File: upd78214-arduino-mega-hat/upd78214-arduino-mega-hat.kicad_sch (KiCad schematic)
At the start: 11 parts, among them J1 Power, J2 PWM, J3 Analog, J4 PWM, J5 Analog, J6 Communication, J7 Digital, U1 upd78214-64p-qfp, Y1 4-12MHz

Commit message: Rambling
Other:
- note added: "PROM read mode needs +12.5V on NMI, ~{RESET} low, ~{CE} and ~{OE} low"
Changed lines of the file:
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@@
+		)
+	)
+	(text "PROM read mode needs +12.5V on NMI, ~{RESET} low, ~{CE} and ~{OE} low"
+		(exclude_from_sim no)
+		(at 226.06 60.96 0)
+		(effects
+			(font
+				(size 1.27 1.27)
+			)
 		)
 	)

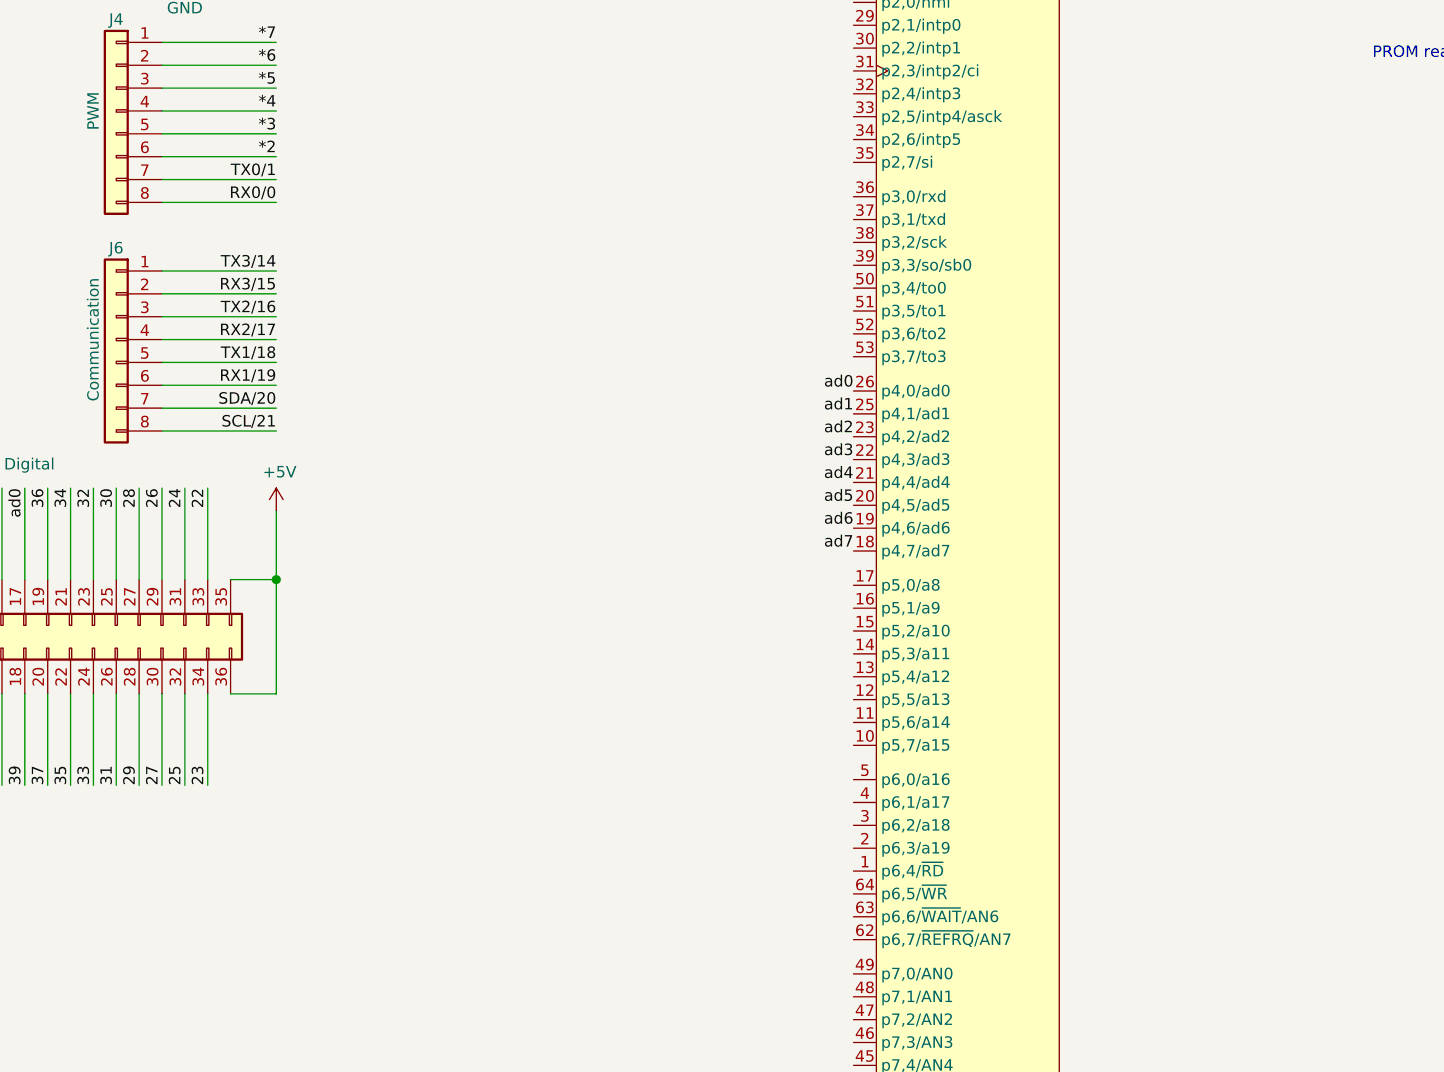
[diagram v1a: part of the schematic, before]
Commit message: TX/RX jumpers, enormous memory products data book
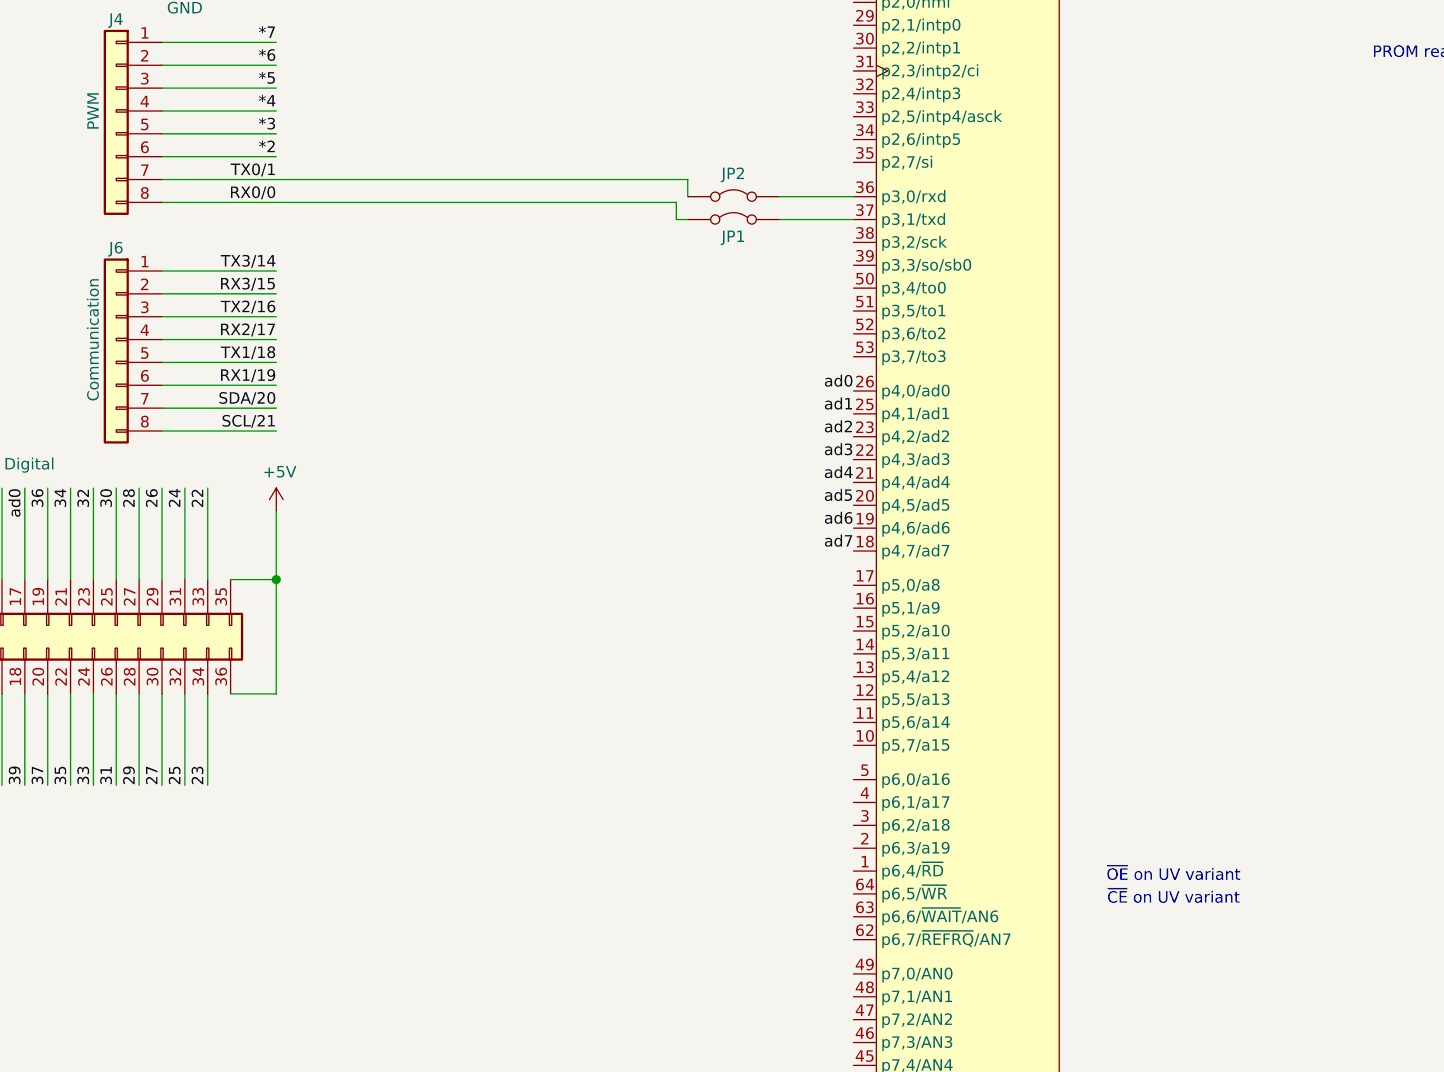
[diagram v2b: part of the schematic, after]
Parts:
- added JP1, JP2: Jumper_2_Bridged, Jumper:SolderJumper-2_P1.3mm_Bridged2Bar_RoundedPad1.0x1.5mm, symbol Jumper:Jumper_2_Bridged
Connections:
- net RX0/0: now also JP1.1 (A)
- net TX0/1: now also JP2.1 (A)
- net at U1.36 (p3,0/rxd): now also JP2.2 (B)
- net at U1.37 (p3,1/txd): now also JP1.2 (B)
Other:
- note added: "~{CE} on UV variant"
- note added: "~{OE} on UV variant"
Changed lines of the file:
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@@
 		)
 	)
+	(text "~{OE} on UV variant"
+		(exclude_from_sim no)
+		(at 174.625 152.4 0)
+		(effects
+			(font
+				(size 1.27 1.27)
+			)
+		)
+	)
 	(text "for both of these:\n30pF 12MHz, 100pF 4MHz"
 		(exclude_from_sim no)
@@
 		)
 	)
+	(text "~{CE} on UV variant"
+		(exclude_from_sim no)
+		(at 174.625 154.94 0)
+		(effects
+			(font
+				(size 1.27 1.27)
+			)
+		)
+	)
 	(text "PROM read mode needs +12.5V on NMI, ~{RESET} low, ~{CE} and ~{OE} low"
 		(exclude_from_sim no)
@@
 	(wire
 		(pts
-			(xy 62.23 77.47) (xy 74.93 77.47)
+			(xy 62.23 77.47) (xy 119.38 77.47)
 		)
 		(stroke
@@
 	(wire
 		(pts
+			(xy 120.65 79.375) (xy 119.38 79.375)
+		)
+		(stroke
+			(width 0)
+			(type default)
+		)
+	)
+	(wire
+		(pts
 			(xy 62.23 44.45) (xy 74.93 44.45)
 		)
@@
 	(wire
 		(pts
+			(xy 119.38 79.375) (xy 119.38 77.47)
+		)
+		(stroke
+			(width 0)
+			(type default)
+		)
+	)
+	(wire
+		(pts
 			(xy 164.465 38.735) (xy 180.975 38.735)
 		)
@@
 	(wire
 		(pts
+			(xy 130.81 76.835) (xy 139.065 76.835)
+		)
+		(stroke
+			(width 0)
+			(type default)
+		)
+	)
+	(wire
+		(pts
 			(xy 180.975 24.765) (xy 206.375 24.765)
 		)
@@
 	(wire
 		(pts
+			(xy 130.81 79.375) (xy 139.065 79.375)
+		)
+		(stroke
+			(width 0)
+			(type default)
+		)
+	)
+	(wire
+		(pts
 			(xy 62.23 39.37) (xy 74.93 39.37)
 		)
@@
 	(wire
 		(pts
+			(xy 120.65 74.93) (xy 120.65 76.835)
+		)
+		(stroke
+			(width 0)
+			(type solid)
+		)
+	)
+	(wire
+		(pts
 			(xy 62.23 87.63) (xy 74.93 87.63)
 		)
@@
 	(wire
 		(pts
-			(xy 62.23 74.93) (xy 74.93 74.93)
+			(xy 62.23 74.93) (xy 120.65 74.93)
 		)
 		(stroke
@@
 	)
 	(symbol
+		(lib_id "Jumper:Jumper_2_Bridged")
+		(at 125.73 79.375 0)
+		(unit 1)
+		(exclude_from_sim no)
+		(in_bom yes)
+		(on_board yes)
+		(dnp no)
+		(property "Reference" "JP1"
+			(at 125.73 81.28 0)
+			(effects
+				(font
+					(size 1.27 1.27)
+				)
+			)
+		)
+		(property "Value" "Jumper_2_Bridged"
+			(at 125.73 76.2 0)
+			(effects
+				(font
+					(size 1.27 1.27)
+				)
+				(hide yes)
+			)
+		)
+		(property "Footprint" "Jumper:SolderJumper-2_P1.3mm_Bridged2Bar_RoundedPad1.0x1.5mm"
+			(at 125.73 79.375 0)
+			(effects
+				(font
+					(size 1.27 1.27)
+				)
+				(hide yes)
+			)
+		)
+		(property "Datasheet" "~"
+			(at 125.73 79.375 0)
+			(effects
+				(font
+					(size 1.27 1.27)
+				)
+				(hide yes)
+			)
+		)
+		(property "Description" "Jumper, 2-pole, closed/bridged"
+			(at 125.73 79.375 0)
+			(effects
+				(font
+					(size 1.27 1.27)
+				)
+				(hide yes)
+			)
+		)
+		(property "DigiKey" ""
+			(at 125.73 79.375 0)
+			(effects
+				(font
+					(size 1.27 1.27)
+				)
+				(hide yes)
+			)
+		)
+		(pin "1"
+		)
+		(pin "2"
+		)
+		(instances
+			(project ""
+				(path "/e63e39d7-6ac0-4ffd-8aa3-1841a4541b55"
+					(reference "JP1")
+					(unit 1)
+				)
+			)
+		)
+	)
+	(symbol
 		(lib_id "NEC:upd78214-64p-qfp")
 		(at 150.495 24.765 0)
@@
 					(unit 1)
 				)
+			)
+		)
+	)
+	(symbol
+		(lib_id "Jumper:Jumper_2_Bridged")
+		(at 125.73 76.835 0)
+		(unit 1)
+		(exclude_from_sim no)
+		(in_bom yes)
+		(on_board yes)
+		(dnp no)
+		(fields_autoplaced yes)
+		(property "Reference" "JP2"
+			(at 125.73 74.295 0)
+			(effects
+				(font
+					(size 1.27 1.27)
+				)
+			)
+		)
+		(property "Value" "Jumper_2_Bridged"
+			(at 125.73 73.66 0)
+			(effects
+				(font
+					(size 1.27 1.27)
+				)
+				(hide yes)
+			)
+		)
+		(property "Footprint" "Jumper:SolderJumper-2_P1.3mm_Bridged2Bar_RoundedPad1.0x1.5mm"
+			(at 125.73 76.835 0)
+			(effects
+				(font
+					(size 1.27 1.27)
+				)
+				(hide yes)
+			)
+		)
+		(property "Datasheet" "~"
+			(at 125.73 76.835 0)
+			(effects
+				(font
+					(size 1.27 1.27)
+				)
+				(hide yes)
+			)
+		)
+		(property "Description" "Jumper, 2-pole, closed/bridged"
+			(at 125.73 76.835 0)
+			(effects
+				(font
+					(size 1.27 1.27)
+				)
+				(hide yes)
+			)
+		)
+		(property "DigiKey" ""
+			(at 125.73 76.835 0)
+			(effects
+				(font
+					(size 1.27 1.27)
+				)
+				(hide yes)
+			)
+		)
+		(pin "1"
+		)
+		(pin "2"
+		)
+		(instances
+			(project "upd78214-arduino-mega-hat"
+				(path "/e63e39d7-6ac0-4ffd-8aa3-1841a4541b55"
+					(reference "JP2")
+					(unit 1)
+				)

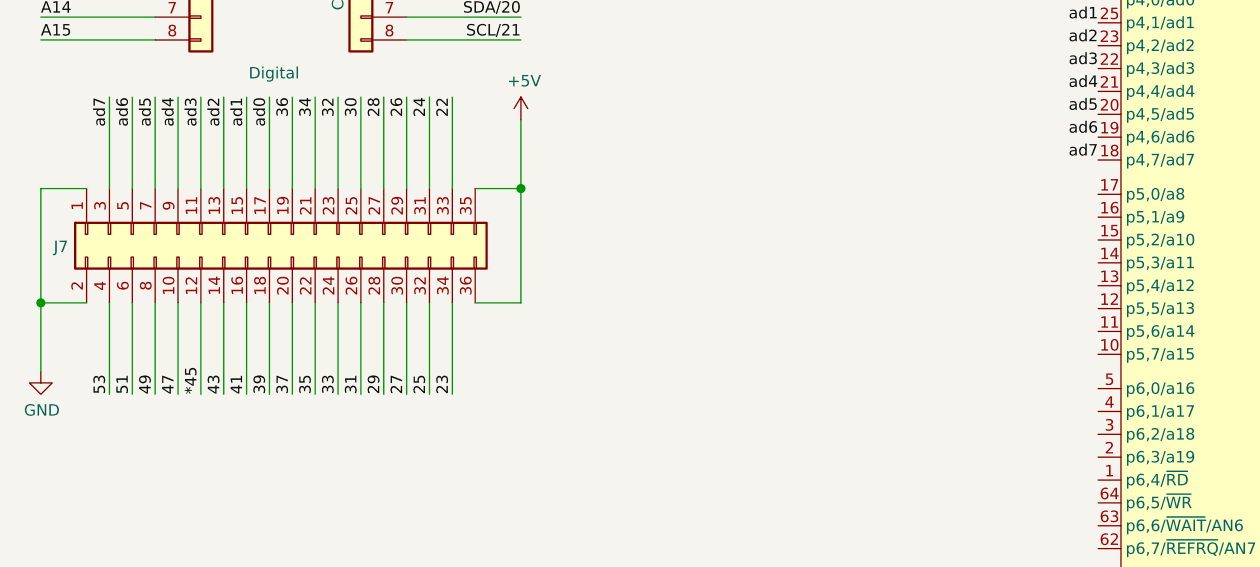
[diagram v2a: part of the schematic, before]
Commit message: Route a8..15
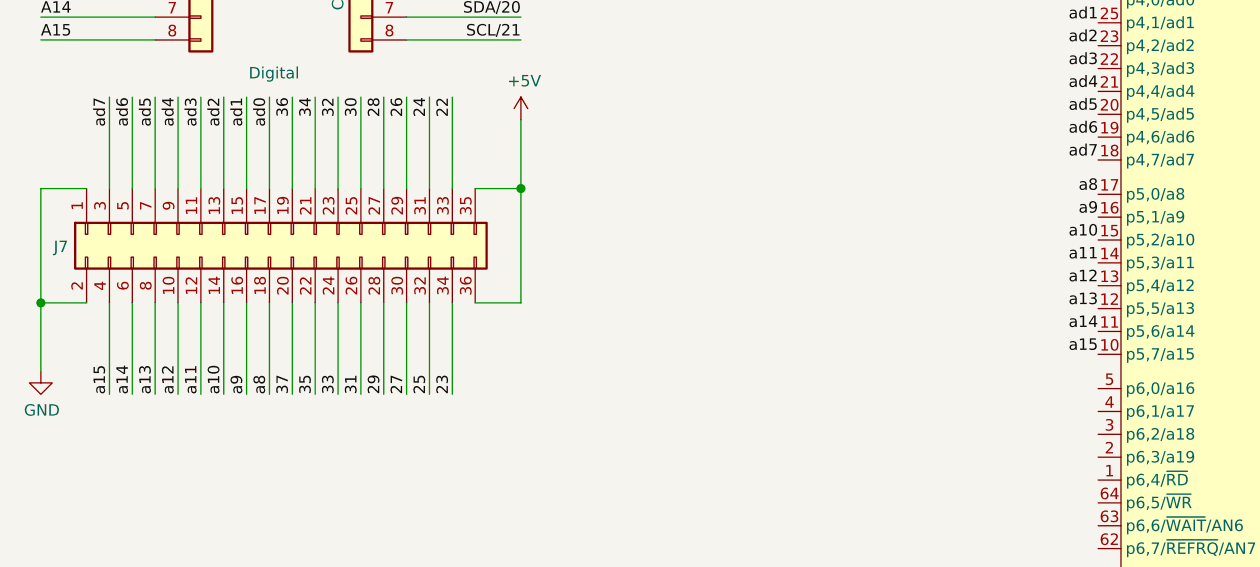
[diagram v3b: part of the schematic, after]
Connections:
- net *45 is gone; now on net a11: J7.12 (Pin_12)
- net 39 is gone; now on net a8: J7.18 (Pin_18)
- net 41 is gone; now on net a9: J7.16 (Pin_16)
- net 43 is gone; now on net a10: J7.14 (Pin_14)
- net 47 is gone; now on net a12: J7.10 (Pin_10)
- net 49 is gone; now on net a13: J7.8 (Pin_8)
- net 51 is gone; now on net a14: J7.6 (Pin_6)
- net 53 is gone; now on net a15: J7.4 (Pin_4)
- net a15: now reaches U1.10 (p5,7/a15)
- net a14: now reaches U1.11 (p5,6/a14)
- net a13: now reaches U1.12 (p5,5/a13)
- net a12: now reaches U1.13 (p5,4/a12)
- net a11: now reaches U1.14 (p5,3/a11)
- net a10: now reaches U1.15 (p5,2/a10)
- net a9: now reaches U1.16 (p5,1/a9)
- net a8: now reaches U1.17 (p5,0/a8)
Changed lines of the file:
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@@
+		)
+	)
+	(label "a12"
+		(at 139.065 130.175 180)
+		(effects
+			(font
+				(size 1.27 1.27)
+			)
+			(justify right bottom)
 		)
 	)
@@
 		)
 	)
+	(label "a15"
+		(at 139.065 137.795 180)
+		(effects
+			(font
+				(size 1.27 1.27)
+			)
+			(justify right bottom)
+		)
+	)
 	(label "31"
 		(at 57.15 142.24 90)
@@
 		)
 	)
+	(label "a14"
+		(at 139.065 135.255 180)
+		(effects
+			(font
+				(size 1.27 1.27)
+			)
+			(justify right bottom)
+		)
+	)
+	(label "a8"
+		(at 139.065 120.015 180)
+		(effects
+			(font
+				(size 1.27 1.27)
+			)
+			(justify right bottom)
+		)
+	)
 	(label "TX1{slash}18"
 		(at 74.93 95.25 180)
@@
 		)
 	)
+	(label "a14"
+		(at 31.75 142.24 90)
+		(effects
+			(font
+				(size 1.27 1.27)
+			)
+			(justify left bottom)
+		)
+	)
 	(label "ad6"
 		(at 139.065 113.665 180)
@@
 		)
 	)
+	(label "a15"
+		(at 29.21 142.24 90)
+		(effects
+			(font
+				(size 1.27 1.27)
+			)
+			(justify left bottom)
+		)
+	)
 	(label "35"
 		(at 52.07 142.24 90)
@@
 		)
 	)
+	(label "a10"
+		(at 139.065 125.095 180)
+		(effects
+			(font
+				(size 1.27 1.27)
+			)
+			(justify right bottom)
+		)
+	)
 	(label "*10"
 		(at 74.93 44.45 180)
@@
 		)
 	)
+	(label "a13"
+		(at 139.065 132.715 180)
+		(effects
+			(font
+				(size 1.27 1.27)
+			)
+			(justify right bottom)
+		)
+	)
+	(label "a12"
+		(at 36.83 142.24 90)
+		(effects
+			(font
+				(size 1.27 1.27)
+			)
+			(justify left bottom)
+		)
+	)
 	(label "23"
 		(at 67.31 142.24 90)
@@
 		)
 	)
+	(label "a11"
+		(at 139.065 127.635 180)
+		(effects
+			(font
+				(size 1.27 1.27)
+			)
+			(justify right bottom)
+		)
+	)
 	(label "A13"
 		(at 21.59 97.79 0)
@@
 		)
 	)
-	(label "41"
-		(at 44.45 142.24 90)
-		(effects
-			(font
-				(size 1.27 1.27)
-			)
-			(justify left bottom)
-		)
-	)
 	(label "30"
 		(at 57.15 109.22 270)
@@
 		)
 	)
-	(label "47"
-		(at 36.83 142.24 90)
-		(effects
-			(font
-				(size 1.27 1.27)
-			)
-			(justify left bottom)
-		)
-	)
 	(label "34"
 		(at 52.07 109.22 270)
@@
 		)
 	)
-	(label "*45"
-		(at 39.37 142.24 90)
-		(effects
-			(font
-				(size 1.27 1.27)
-			)
-			(justify left bottom)
-		)
-	)
 	(label "ad0"
 		(at 46.99 109.22 270)
@@
 		)
 	)
-	(label "51"
-		(at 31.75 142.24 90)
+	(label "a8"
+		(at 46.99 142.24 90)
 		(effects
 			(font
@@
 		)
 	)
-	(label "53"
-		(at 29.21 142.24 90)
-		(effects
-			(font
-				(size 1.27 1.27)
-			)
-			(justify left bottom)
-		)
-	)
 	(label "TX0{slash}1"
 		(at 74.93 74.93 180)
@@
 		)
 	)
+	(label "a9"
+		(at 44.45 142.24 90)
+		(effects
+			(font
+				(size 1.27 1.27)
+			)
+			(justify left bottom)
+		)
+	)
 	(label "24"
 		(at 64.77 109.22 270)
@@
 		)
 	)
+	(label "a11"
+		(at 39.37 142.24 90)
+		(effects
+			(font
+				(size 1.27 1.27)
+			)
+			(justify left bottom)
+		)
+	)
 	(label "A0"
 		(at 21.59 59.69 0)
@@
 		)
 	)
-	(label "39"
-		(at 46.99 142.24 90)
-		(effects
-			(font
-				(size 1.27 1.27)
-			)
-			(justify left bottom)
-		)
-	)
 	(label "A8"
 		(at 21.59 85.09 0)
@@
 		)
 	)
+	(label "a9"
+		(at 139.065 122.555 180)
+		(effects
+			(font
+				(size 1.27 1.27)
+			)
+			(justify right bottom)
+		)
+	)
 	(label "*5"
 		(at 74.93 64.77 180)
@@
 		)
 	)
+	(label "a10"
+		(at 41.91 142.24 90)
+		(effects
+			(font
+				(size 1.27 1.27)
+			)
+			(justify left bottom)
+		)
+	)
 	(label "IOREF"
 		(at 19.05 34.29 0)
@@
 		)
 	)
-	(label "49"
-		(at 34.29 142.24 90)
-		(effects
-			(font
-				(size 1.27 1.27)
-			)
-			(justify left bottom)
-		)
-	)
 	(label "A5"
 		(at 21.59 72.39 0)
@@
 		)
 	)
+	(label "a13"
+		(at 34.29 142.24 90)
+		(effects
+			(font
+				(size 1.27 1.27)
+			)
+			(justify left bottom)
+		)
+	)
 	(label "ad0"
 		(at 139.065 98.425 180)
@@
 		)
 	)
-	(label "43"
-		(at 41.91 142.24 90)
-		(effects
-			(font
-				(size 1.27 1.27)
-			)
-			(justify left bottom)
-		)
-	)
